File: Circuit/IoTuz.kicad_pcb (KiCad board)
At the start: 2 copper layers, 150 x 95 mm, 95 parts, among them P1 ALLIGATOR_01X35, P2 BATTERY, P3 USB_5PIN_SHELL, P4 LED_1, P5 LED_2, P8 IRReceiver, Q1 S8050, Q2 S8050, Q202 FDN340P, Q203 FDN340P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

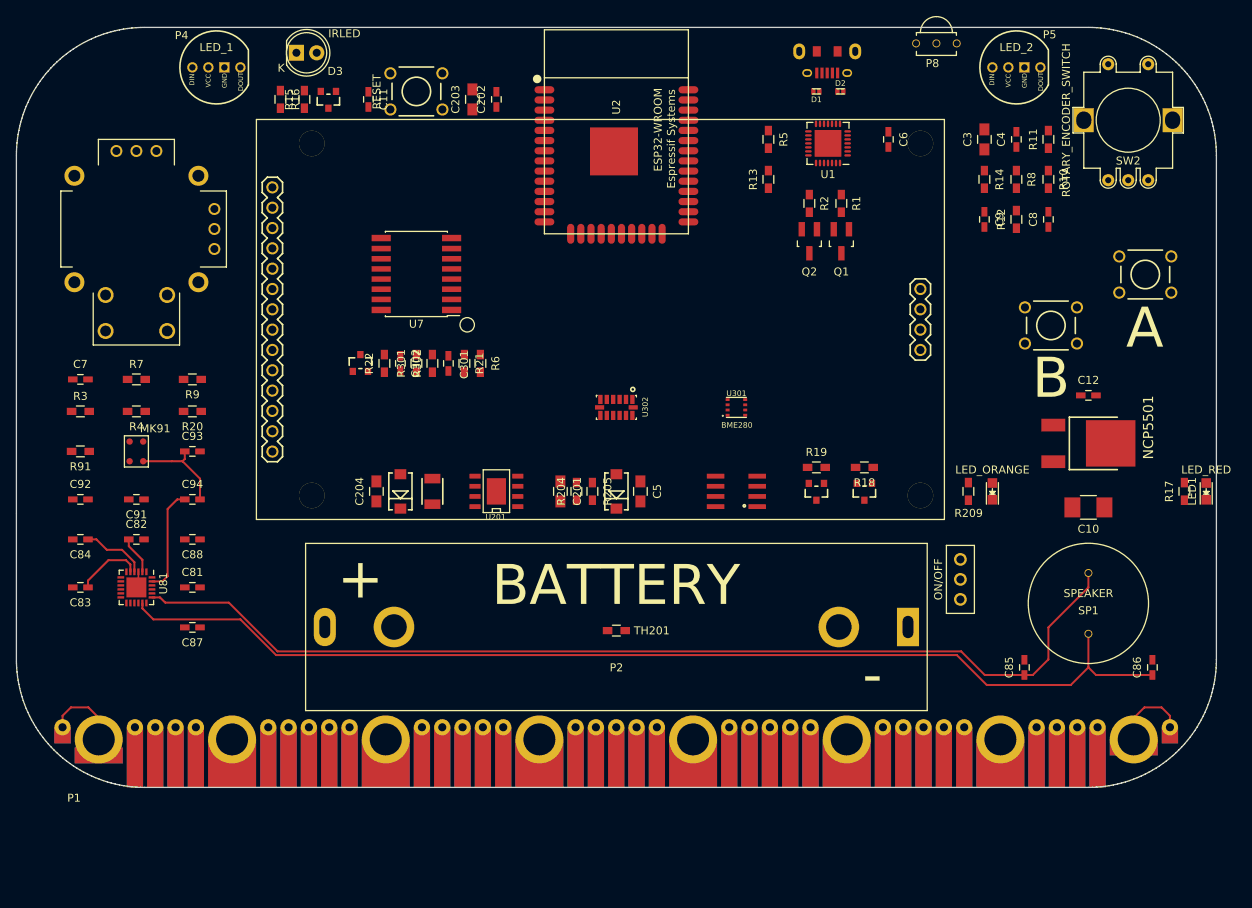
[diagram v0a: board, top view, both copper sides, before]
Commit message: F.CU & B.CU fills. Need to modify or remove parts of F.Cu.
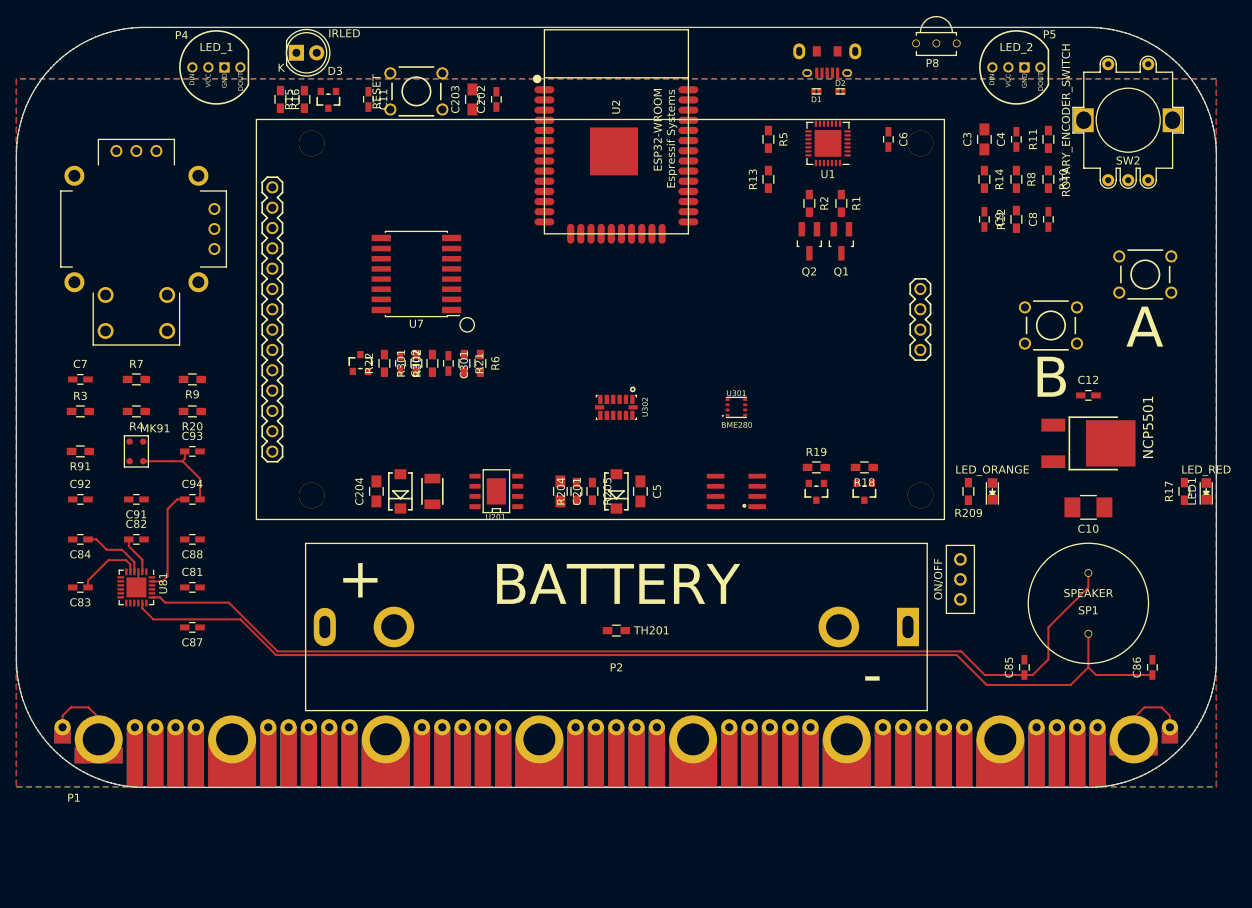
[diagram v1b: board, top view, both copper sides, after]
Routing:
- added copper zone on F.Cu, net +3V3
- added copper zone on B.Cu, net GND
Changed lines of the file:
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@@
     (links 396)
     (no_connects 297)
-    (area 49.949999 54.949999 200.050001 150.050001)
+    (area 0 34.300001 202.169477 152.451)
     (thickness 1.6)
     (drawings 234)
@@
   (layers
     (0 F.Cu signal)
-    (31 B.Cu signal)
+    (31 B.Cu signal hide)
     (32 B.Adhes user)
     (33 F.Adhes user)
@@
   )
   (setup
-    (last_trace_width 0.254)
+    (last_trace_width 0.2032)
     (user_trace_width 0.254)
     (user_trace_width 0.3048)
@@
     (aux_axis_origin 50 150)
     (grid_origin 50 150)
-    (visible_elements 7FFFFFFF)
+    (visible_elements 7FFFF7FF)
     (pcbplotparams
       (layerselection 0x31ef0_80000001)
@@
       )
     )
+  )
+  (zone (net 1) (net_name +3V3) (layer F.Cu) (hatch edge 0.508)
+    (connect_pads (clearance 0.508))
+    (min_thickness 0.254)
+    (fill yes (arc_segments 16) (thermal_gap 0.508) (thermal_bridge_width 0.508))
+    (polygon
+      (pts
+        (xy 116 61.5) (xy 50 61.5) (xy 50 150) (xy 200 150) (xy 200 61.5)
+      )
+    )
+  )
+  (zone (net 2) (net_name GND) (layer B.Cu) (hatch edge 0.508)
+    (connect_pads (clearance 0.508))
+    (min_thickness 0.254)
+    (fill yes (arc_segments 16) (thermal_gap 0.508) (thermal_bridge_width 0.508))
+    (polygon
+      (pts
+        (xy 116 61.404026) (xy 50 61.404026) (xy 50 149.904026) (xy 200 149.904026) (xy 200 61.404026)
+      )
+    )

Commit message: Testing. Nearly there with fills & stitching.
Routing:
- net +5V: track 9.64 -> 236.0 mm, vias 0 -> 4
- net /I2C_SCL: track 0.00 -> 219.2 mm, vias 0 -> 3
- net GND: track 11.7 -> 212.0 mm, vias 0 -> 48
- net /I2C_SDA: track 0.00 -> 199.8 mm, vias 0 -> 3
- net /IO13: track 0.00 -> 197.8 mm, vias 0 -> 1
- net /IO14: track 0.00 -> 180.7 mm, vias 0 -> 1
- net /IO18: track 0.00 -> 180.1 mm, vias 0 -> 1
- net /IO5: track 0.00 -> 174.3 mm, vias 0 -> 4
- net /IO23: track 0.00 -> 172.2 mm, vias 0 -> 1
- net /IO17: track 0.00 -> 170.9 mm, vias 0 -> 1
- net /IO0: track 0.00 -> 166.3 mm, vias 0 -> 3
- net /IO16: track 0.00 -> 160.5 mm, vias 0 -> 2
- net /IO12: track 0.00 -> 159.0 mm, vias 0 -> 3
- net /IO26: track 0.00 -> 153.0 mm
- net /IO34: track 0.00 -> 151.4 mm
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- added copper zone on F.Cu, net GND
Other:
- net class CurrentCarry: trace_width 0.25 -> 0.254
- net class GroundBlock added: clearance 0.508, trace_width 0.2032, via_dia 0.6, via_drill 0.4

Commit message: Fixing up pours.
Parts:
- added REF**: via.0.6mm-drill.0.4mm, libs:via.0.6mm-drill.0.4mm, F.Cu at (100.0, 135.8)
- added REF**: via.0.6mm-drill.0.4mm, libs:via.0.6mm-drill.0.4mm, F.Cu at (113.2, 135.8)
- added REF**: via.0.6mm-drill.0.4mm, libs:via.0.6mm-drill.0.4mm, F.Cu at (122.5, 135.8)
- moved C203 88.2 mm to (171.6, 124.0)
- moved C202 87.7 mm to (174.0, 124.0)
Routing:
- net +3V3: track 45.3 -> 84.4 mm, vias 0 -> 4
- net GND: track 212.0 -> 241.4 mm
- net /Power/3.3V: track 138.2 -> 144.8 mm
- net /I2C_SCL: track 219.2 -> 223.7 mm
- net /IO26: track 153.0 -> 154.9 mm
- net /IO5: track 174.3 -> 176.0 mm
- net /I2C_SDA: track 199.8 -> 200.8 mm
- net /BL_Control: track 17.5 -> 18.3 mm

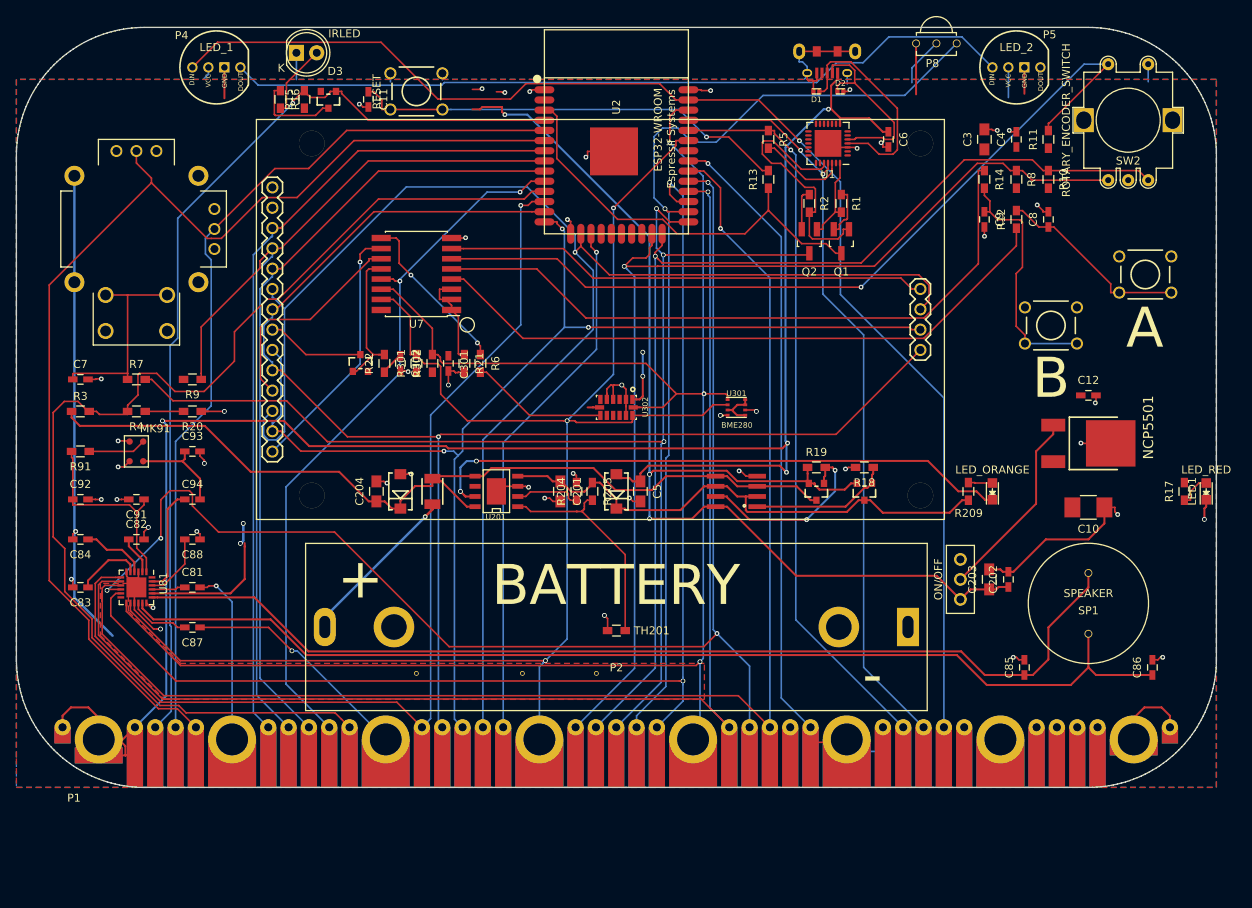
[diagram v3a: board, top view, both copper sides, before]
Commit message: Most routing done, some pours and tracks to clean up.
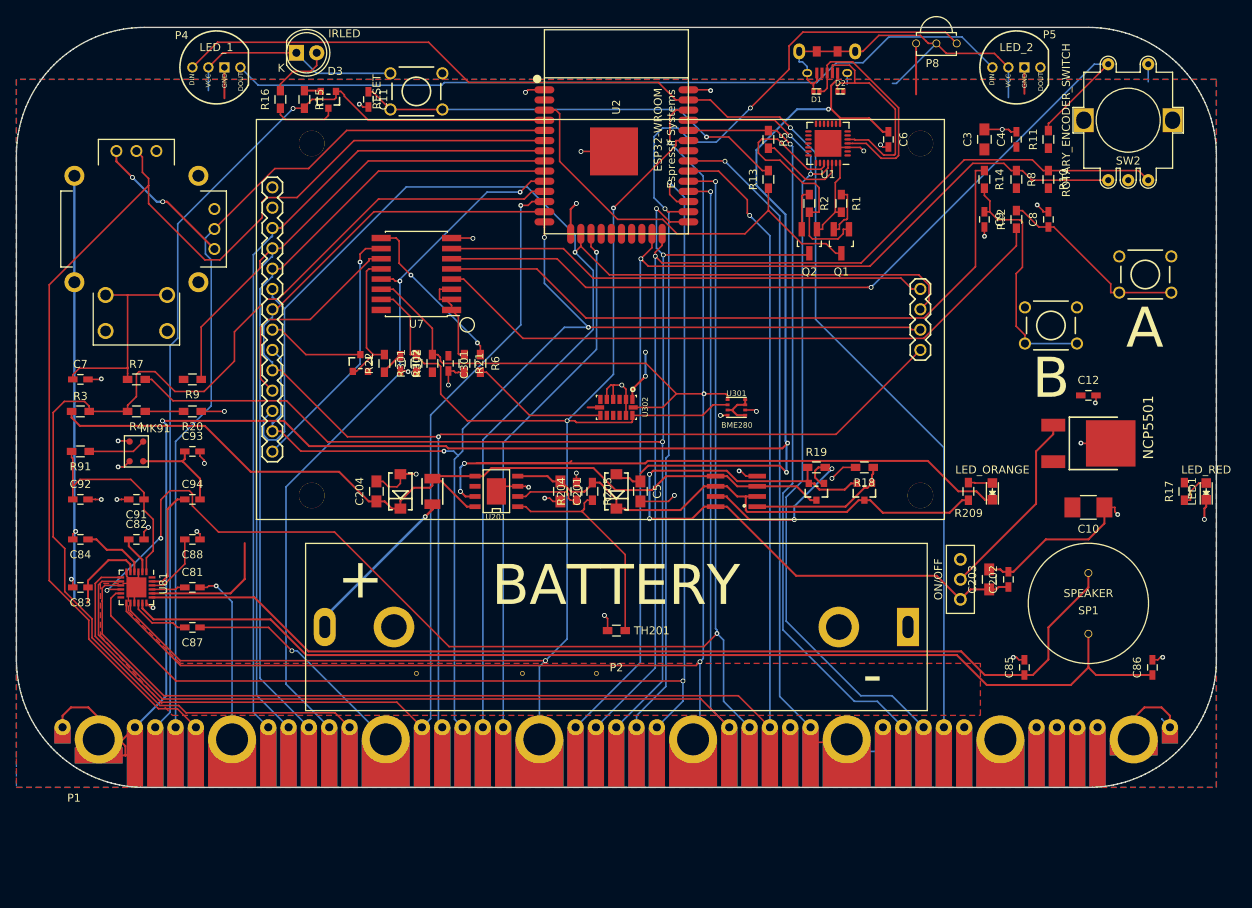
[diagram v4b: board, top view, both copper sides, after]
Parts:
- turned R15 to 270 degrees
- turned R16 to 90 degrees
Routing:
- net /Power/3.3V: track 144.8 -> 85.8 mm, vias 3 -> 2
- net GND: track 241.4 -> 286.9 mm, vias 48 -> 42
- net +3V3: track 84.4 -> 101.1 mm
- net (no net): track 0.00 -> 12.0 mm
- net /RXD: track 103.2 -> 109.8 mm
- net /IO34: track 151.7 -> 156.3 mm
- net +5V: track 236.0 -> 240.0 mm
- net /USB_D-: track 23.6 -> 27.5 mm
- net /IO15: track 141.9 -> 138.3 mm
- net /IO4: track 131.0 -> 133.9 mm, vias 1 -> 2
- net /TXD: track 99.5 -> 102.4 mm
- net Net-(Q4-PadD): track 10.9 -> 8.16 mm
- net /RTS: track 32.3 -> 34.4 mm
- net /Audio/MICBias: track 25.0 -> 26.8 mm
- net /IO19: track 108.4 -> 109.8 mm
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
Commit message: A few more routing touch-ups.
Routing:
- net +3V3: track 101.1 -> 134.4 mm, vias 4 -> 8
- net (no net): track 12.0 -> 0.00 mm
- net GND: track 286.9 -> 293.2 mm
- net Net-(R205-Pad2): track 28.2 -> 33.9 mm
- net /IO34: track 156.3 -> 160.6 mm
- net /BAT+: track 111.8 -> 115.4 mm
- net +5V: track 240.0 -> 242.5 mm
- net /IO13: track 197.8 -> 199.4 mm
- net /Power/3.3V: track 85.8 -> 87.1 mm
- net /Touch_INT: track 32.1 -> 33.0 mm

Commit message: Routing detail.:
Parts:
- moved C301 4.00 mm to (100.0, 97.0)
- moved R301 2.00 mm to (102.0, 97.0)
- moved R302 2.00 mm to (104.0, 97.0)
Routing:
- net GND: track 293.2 -> 290.7 mm, vias 42 -> 41
- net /I2C_SCL: track 222.6 -> 221.3 mm
- net +3V3: track 134.4 -> 135.4 mm
- net /I2C_SDA: track 200.8 -> 201.4 mm

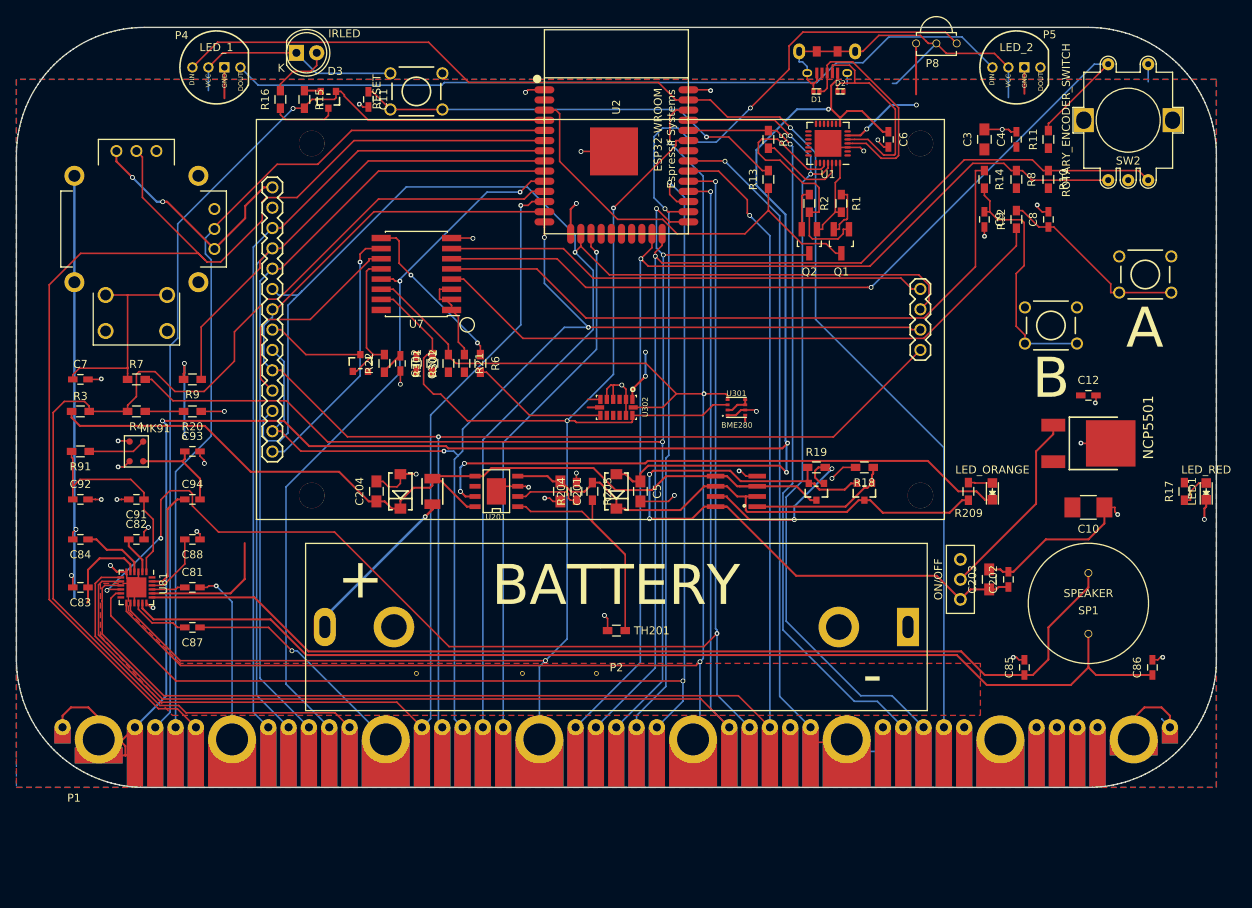
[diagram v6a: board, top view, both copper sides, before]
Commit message: Just caught I/O error on controller sch. XY reversed.
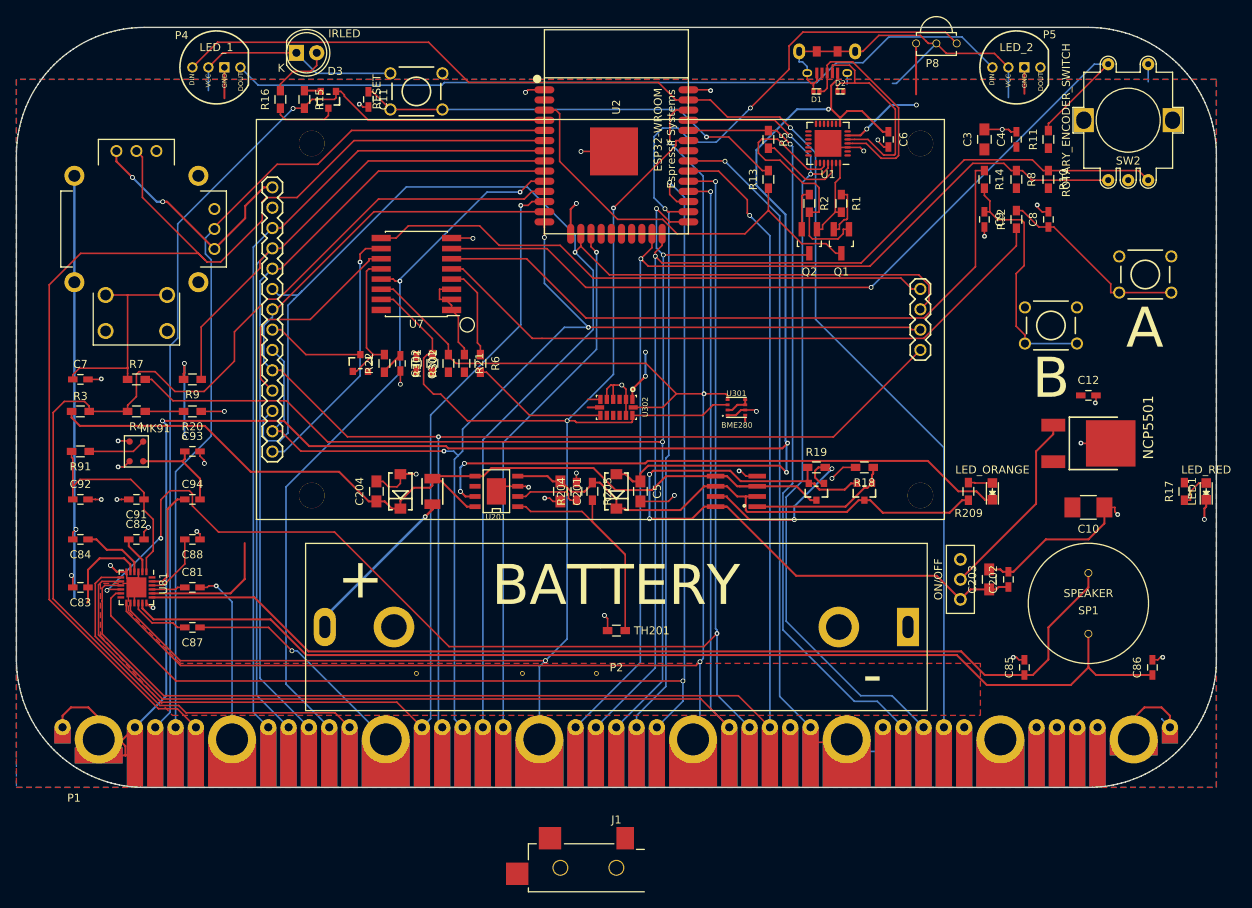
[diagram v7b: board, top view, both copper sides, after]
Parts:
- added J1: Jack.3.5mm-Mono, libs:3.5mmMonoTSJack.MJ-3523-SMT.Switch, F.Cu at (125.0, 160.1)
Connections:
- U7 pad 4: /A_Btn -> /ACCEL_INT
- U7 pad 5: /B_Btn -> /A_Btn
- U7 pad 6: /Enc_Btn -> /B_Btn
- U7 pad 7: /SD_Sel -> /Enc_Btn
- U7 pad 9: /ACCEL_INT -> /SD_Sel
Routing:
- net /SD_Sel: track 60.7 -> 71.3 mm
- net /ACCEL_INT: track 20.8 -> 11.8 mm, vias 2 -> 0
- net /Enc_Btn: track 106.6 -> 107.1 mm
- net /B_Btn: track 83.8 -> 84.3 mm
- net /A_Btn: track 80.7 -> 81.2 mm

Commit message: Changing one or two nets.
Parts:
- removed J1: Jack.3.5mm-Mono, libs:3.5mmMonoTSJack.MJ-3523-SMT.Switch
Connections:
- U4 pad X2: /Sensor_VN -> /IO34
- U4 pad Y2: /IO34 -> /Sensor_VN
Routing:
- net +3V3: track 135.5 -> 105.6 mm, vias 8 -> 6
- net /Sensor_VN: track 118.9 -> 142.5 mm
- net Net-(R205-Pad2): track 33.9 -> 18.0 mm
- net /IO34: track 160.6 -> 148.5 mm
- net GND: track 290.7 -> 289.4 mm
- net +5V: track 242.5 -> 241.9 mm
